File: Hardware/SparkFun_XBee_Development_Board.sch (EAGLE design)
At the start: 80 parts, among them J1 USB Female Type C Connector, J3 USB Female Type C Connector, J4 QWIIC_RIGHT_ANGLE, Q2 3.1A/30V/105mΩ, U1 FSUSB30MUX_MSOP10, U2 AP63203, U3 ESD Diode, U4 MCP73831, U5 ESD Diode, U7 FT231XS

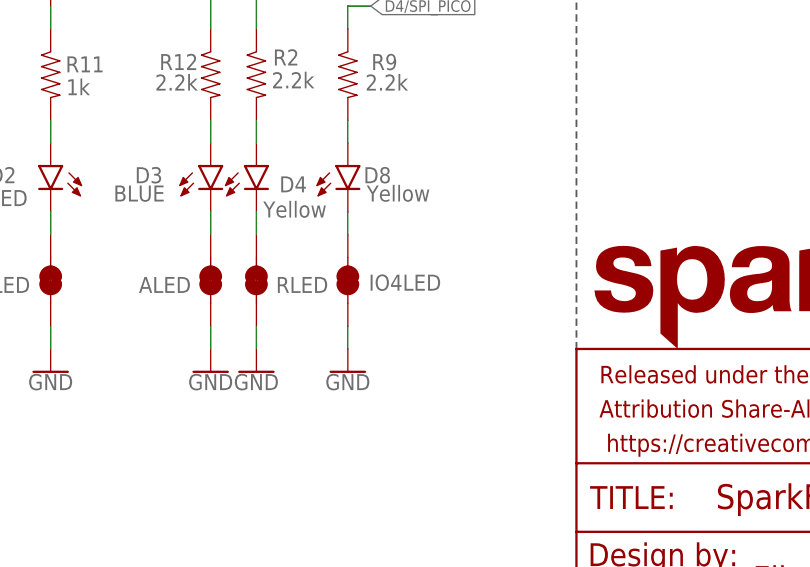
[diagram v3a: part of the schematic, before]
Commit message: Changes silk on IOLED jumper
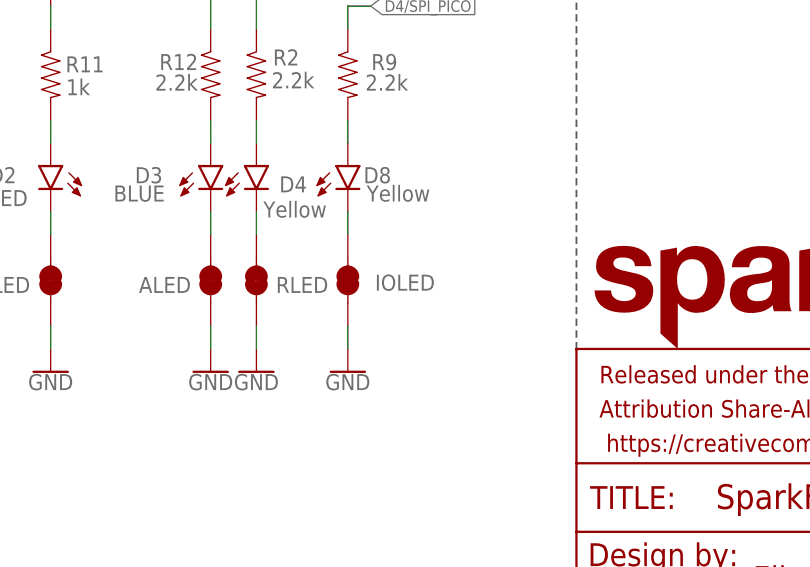
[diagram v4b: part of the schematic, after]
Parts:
- renumbered IO4LED to IOLED
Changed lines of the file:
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@@
 <part name="R9" library="SparkFun-Resistors" deviceset="2.2KOHM" device="-0603-1/10W-1%" value="2.2k"/>
 <part name="GND42" library="SparkFun-PowerSymbols" deviceset="GND" device=""/>
-<part name="IO4LED" library="SparkFun-Jumpers" deviceset="JUMPER-SMT_2_NC_TRACE" device="_SILK" package3d_urn="urn:adsk.eagle:package:39281/1"/>
+<part name="IOLED" library="SparkFun-Jumpers" deviceset="JUMPER-SMT_2_NC_TRACE" device="_SILK" package3d_urn="urn:adsk.eagle:package:39281/1"/>
 </parts>
 <sheets>
@@
 <attribute name="VALUE" x="304.8" y="32.766" size="1.778" layer="96" font="vector" align="top-center"/>
 </instance>
-<instance part="IO4LED" gate="G$1" x="304.8" y="43.18" smashed="yes" rot="R90">
+<instance part="IOLED" gate="G$1" x="304.8" y="43.18" smashed="yes" rot="R90">
 <attribute name="NAME" x="311.15" y="42.926" size="1.778" layer="95" font="vector" rot="R180" align="center"/>
 </instance>
@@
 </segment>
 <segment>
-<pinref part="IO4LED" gate="G$1" pin="1"/>
+<pinref part="IOLED" gate="G$1" pin="1"/>
 <pinref part="GND42" gate="1" pin="GND"/>
 <wire x1="304.8" y1="38.1" x2="304.8" y2="35.56" width="0.1524" layer="91"/>
@@
 <net name="RLED1" class="0">
 <segment>
-<pinref part="IO4LED" gate="G$1" pin="2"/>
+<pinref part="IOLED" gate="G$1" pin="2"/>
 <pinref part="D8" gate="G$1" pin="C"/>
 <wire x1="304.8" y1="48.26" x2="304.8" y2="50.8" width="0.1524" layer="91"/>

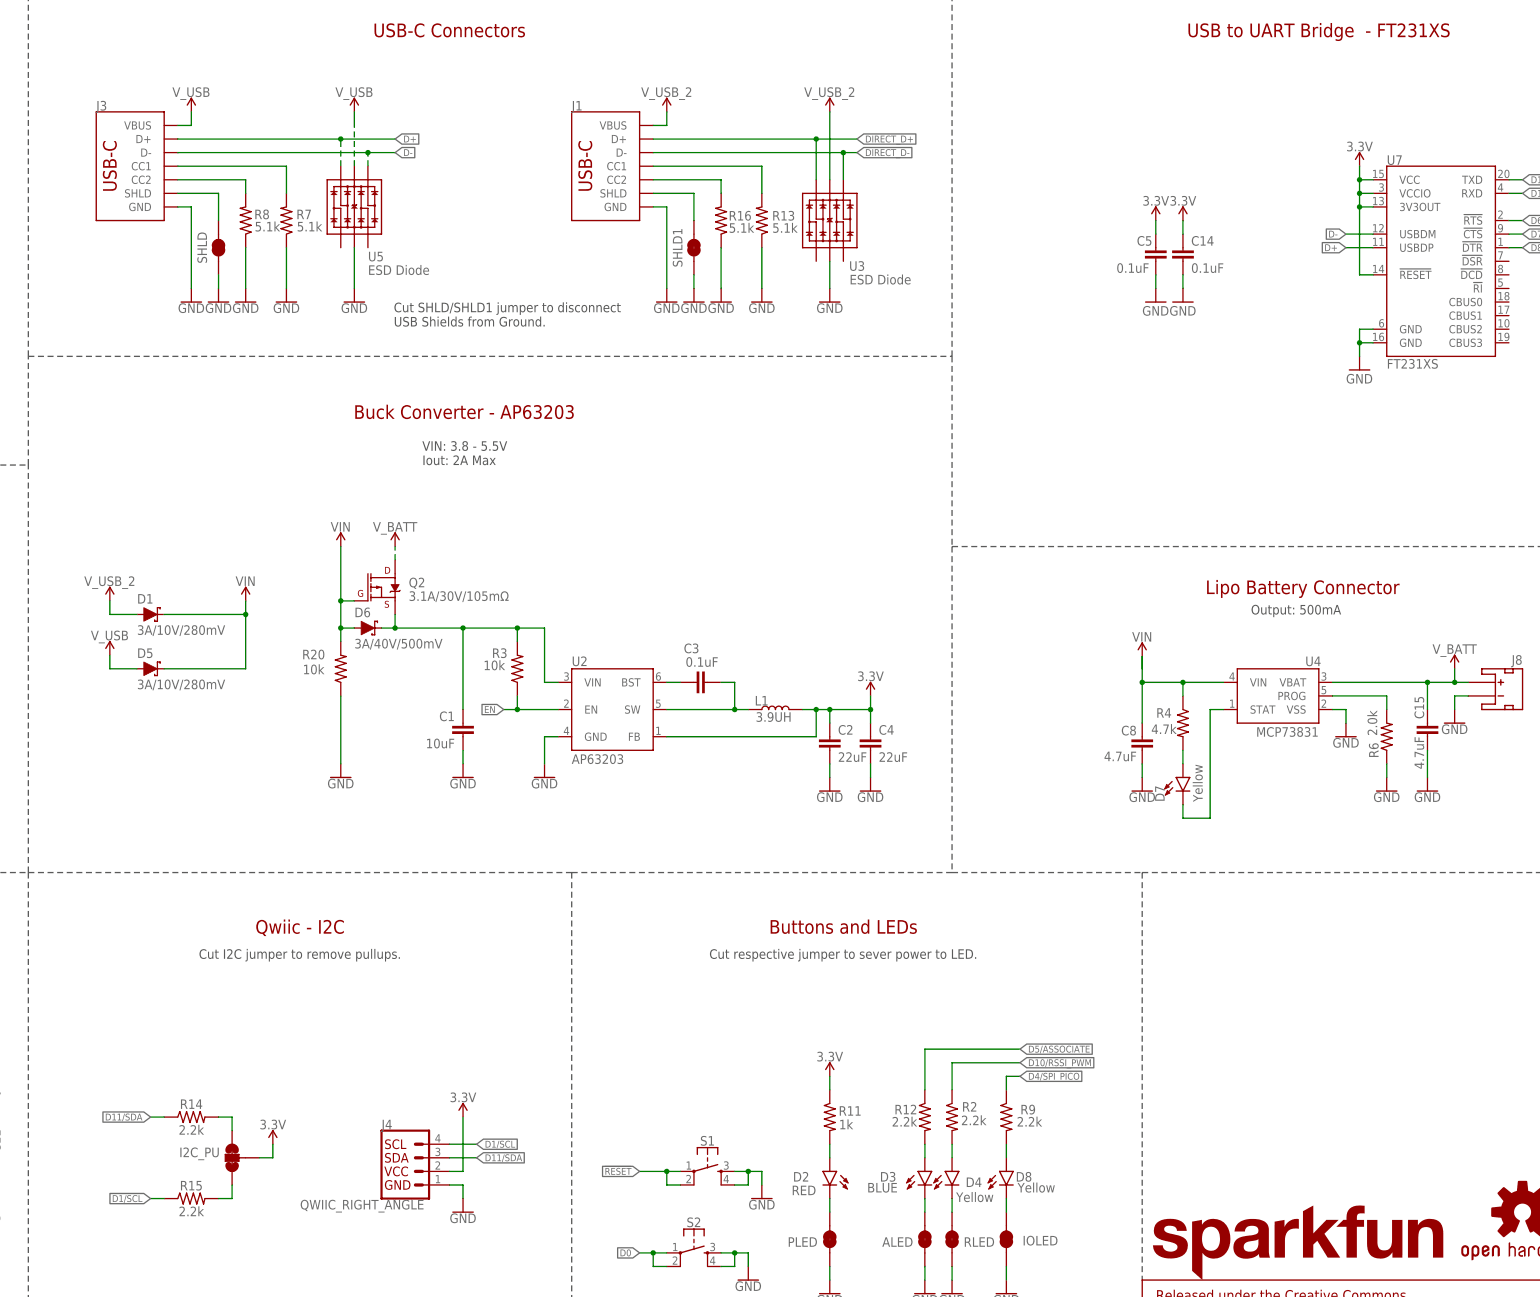
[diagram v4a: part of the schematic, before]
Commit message: Swaps yellow user LED for a green one
* Improves copper pour
* Fixes some whacky traces
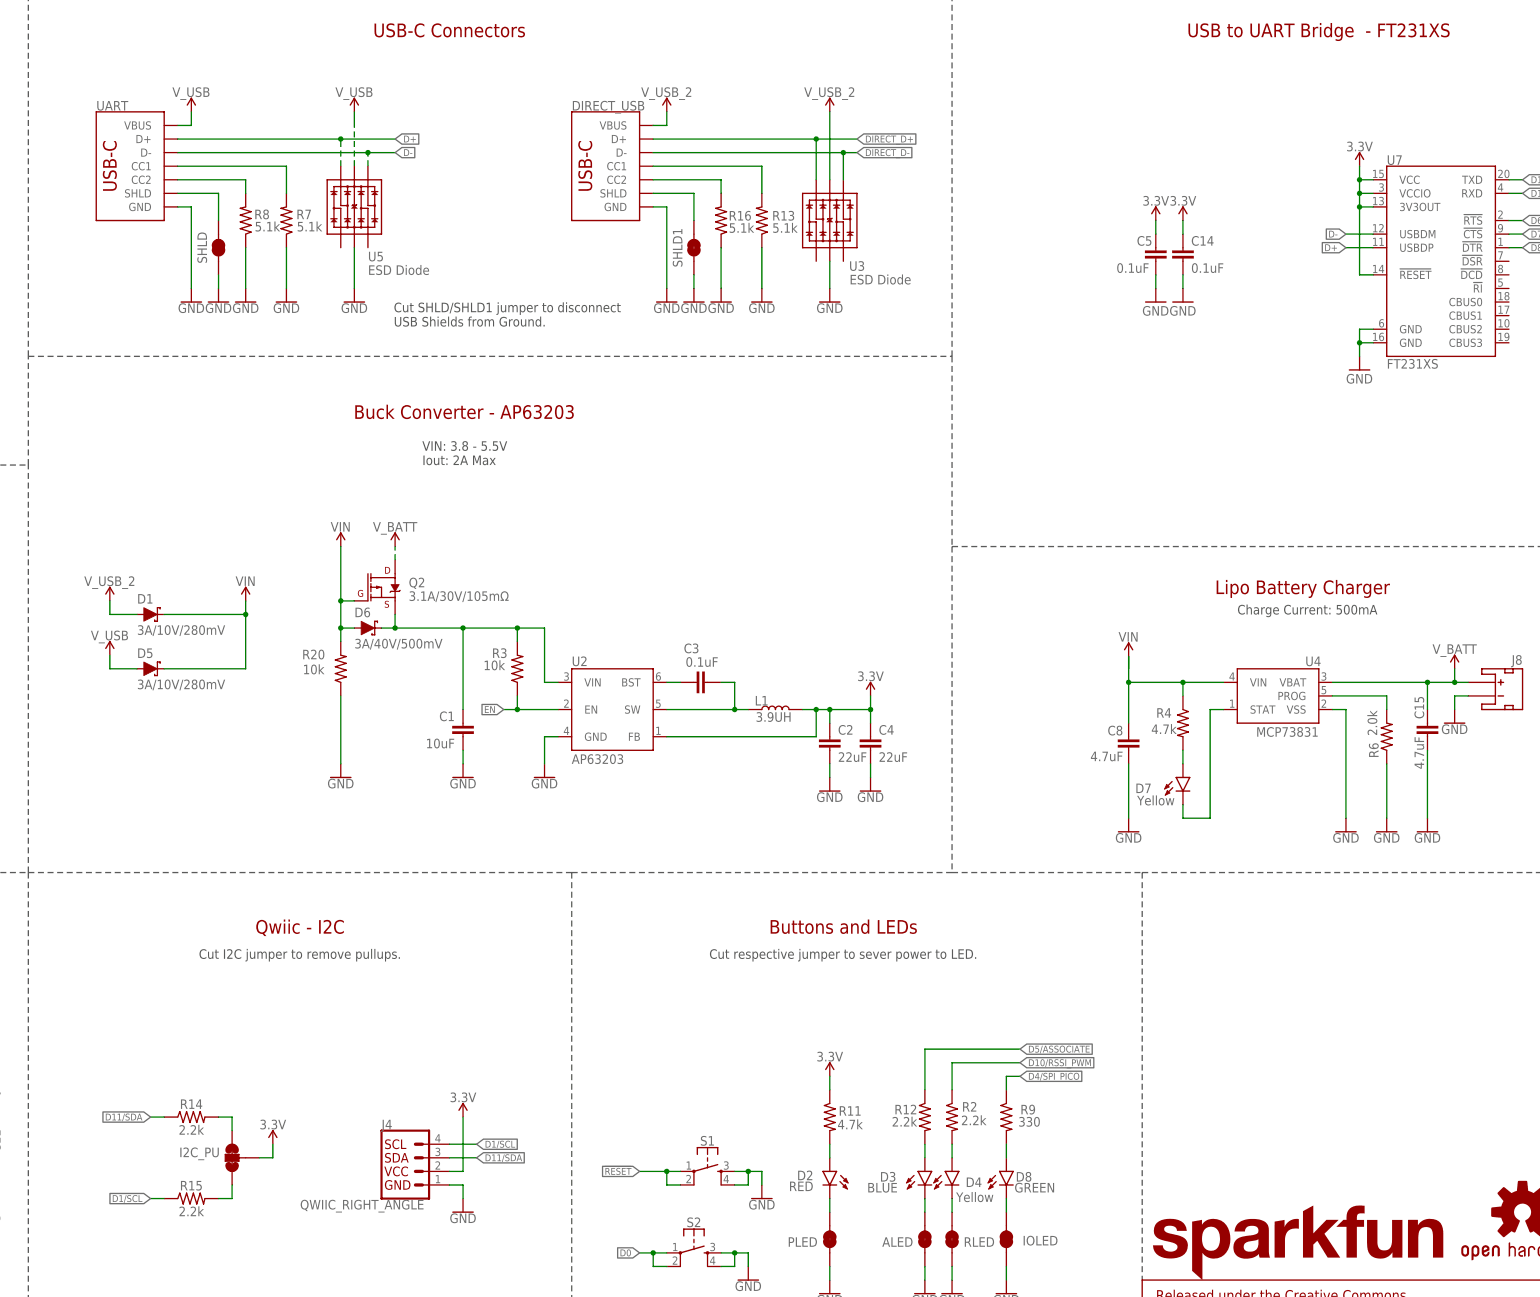
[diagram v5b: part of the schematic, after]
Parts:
- D2: device SparkFun-LED:LED-RED0603 -> SparkFun-LED:LED-RED_0603-KB
- D8: value Yellow -> GREEN; device SparkFun-LED:LED-YELLOW0603 -> SparkFun-LED:LED-GREEN0603
- R11: value 1k -> 4.7k; device SparkFun-Resistors:1KOHM-0603-1/10W-1% -> SparkFun-Resistors:4.7KOHM-0603-1/10W-1%
- R9: value 2.2k -> 330; device SparkFun-Resistors:2.2KOHM-0603-1/10W-1% -> SparkFun-Resistors:330OHM-0603-1/10W-1%
- renumbered J1 to DIRECT_USB, J3 to UART
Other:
- note added: "Charge Current: 500mA"
- note added: "Lipo Battery Charger"
- note removed: "Lipo Battery Connector"
- note removed: "Output: 500mA"
- moved on the sheet: C8

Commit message: Updates production panel
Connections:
- net RLED1 renamed IOLED
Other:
- moved on the sheet: ALED, C11, C15, C8, D3, D4, D7, D8, IOLED, J12, J8, R12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
